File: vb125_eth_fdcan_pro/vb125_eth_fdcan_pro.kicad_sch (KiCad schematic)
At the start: 0 parts

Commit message: Finish schematics.
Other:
- sheet Bus Power ports: added +VIN_DB9; removed none
- sheet CAN Ch1 ports: added +VIN_DB9, FDCAN_RX, FDCAN_TX, TERM_DIS, TERM_EN; removed none
- sheet CAN Ch2: file p7_can_ch2.kicad_sch -> p6_can_ch1.kicad_sch
- sheet CAN Ch2 ports: added FDCAN_RX, FDCAN_TX, TERM_DIS, TERM_EN; removed none
- sheet MCU_H7 ports: added FDCAN1_RX, FDCAN1_TX, FDCAN3_RX, FDCAN3_TX, TERM1_DIS, TERM1_EN, TERM2_DIS, TERM2_EN; removed none
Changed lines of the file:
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@@
     (company "vhrd.tech")
+  )
+  (wire (pts (xy 119.38 90.17) (xy 127 90.17))
+    (stroke (width 0) (type default))
+  )
+  (wire (pts (xy 119.38 92.71) (xy 127 92.71))
+    (stroke (width 0) (type default))
+  )
+  (wire (pts (xy 119.38 111.76) (xy 127 111.76))
+    (stroke (width 0) (type default))
+  )
+  (wire (pts (xy 119.38 114.3) (xy 127 114.3))
+    (stroke (width 0) (type default))
+  )
+  (wire (pts (xy 158.75 106.68) (xy 170.18 106.68))
+    (stroke (width 0) (type default))
+  )
+  (wire (pts (xy 119.38 105.41) (xy 127 105.41))
+    (stroke (width 0) (type default))
+  )
+  (wire (pts (xy 119.38 83.82) (xy 127 83.82))
+    (stroke (width 0) (type default))
+  )
+  (wire (pts (xy 119.38 86.36) (xy 127 86.36))
+    (stroke (width 0) (type default))
+  )
+  (wire (pts (xy 119.38 107.95) (xy 127 107.95))
+    (stroke (width 0) (type default))
   )
   (text_box "TODO:\n--\nabc\n"
@@
     )
   )
-  (sheet (at 170.18 115.57) (size 31.75 7.62) (fields_autoplaced)
-    (stroke (width 0.1524) (type solid))
-    (fill (color 0 0 0 0.0000))
-    (property "Sheetname" "Bus Power" (at 170.18 114.8584 0)
-      (effects (font (size 1.27 1.27)) (justify left bottom))
-    )
-    (property "Sheetfile" "p9_bus_power.kicad_sch" (at 170.18 123.7746 0)
-      (effects (font (size 1.27 1.27)) (justify left top))
+  (sheet (at 127 81.28) (size 31.75 13.97) (fields_autoplaced)
+    (stroke (width 0.1524) (type solid))
+    (fill (color 0 0 0 0.0000))
+    (property "Sheetname" "CAN Ch2" (at 127 80.5684 0)
+      (effects (font (size 1.27 1.27)) (justify left bottom))
+    )
+    (property "Sheetfile" "p6_can_ch1.kicad_sch" (at 127 95.8346 0)
+      (effects (font (size 1.27 1.27)) (justify left top))
+    )
+    (pin "FDCAN_TX" input (at 127 83.82 180)
+      (effects (font (size 1.27 1.27)) (justify left))
+    )
+    (pin "FDCAN_RX" output (at 127 86.36 180)
+      (effects (font (size 1.27 1.27)) (justify left))
+    )
+    (pin "TERM_EN" input (at 127 90.17 180)
+      (effects (font (size 1.27 1.27)) (justify left))
+    )
+    (pin "TERM_DIS" input (at 127 92.71 180)
+      (effects (font (size 1.27 1.27)) (justify left))
+    )
+    (instances
+      (project "vb125_eth_fdcan_pro"
+        (path "/b473bccb-f14c-41d5-b473-137d3ef8ae1e" (page "7"))
+      )
+    )
+  )
+  (sheet (at 170.18 102.87) (size 31.75 7.62) (fields_autoplaced)
+    (stroke (width 0.1524) (type solid))
+    (fill (color 0 0 0 0.0000))
+    (property "Sheetname" "Bus Power" (at 170.18 102.1584 0)
+      (effects (font (size 1.27 1.27)) (justify left bottom))
+    )
+    (property "Sheetfile" "p9_bus_power.kicad_sch" (at 170.18 111.0746 0)
+      (effects (font (size 1.27 1.27)) (justify left top))
+    )
+    (pin "+VIN_DB9" input (at 170.18 106.68 180)
+      (effects (font (size 1.27 1.27)) (justify left))
     )
     (instances
@@
     )
   )
-  (sheet (at 170.18 100.33) (size 31.75 7.62) (fields_autoplaced)
-    (stroke (width 0.1524) (type solid))
-    (fill (color 0 0 0 0.0000))
-    (property "Sheetname" "PoE" (at 170.18 99.6184 0)
-      (effects (font (size 1.27 1.27)) (justify left bottom))
-    )
-    (property "Sheetfile" "p8_poe.kicad_sch" (at 170.18 108.5346 0)
+  (sheet (at 170.18 118.11) (size 31.75 7.62) (fields_autoplaced)
+    (stroke (width 0.1524) (type solid))
+    (fill (color 0 0 0 0.0000))
+    (property "Sheetname" "PoE" (at 170.18 117.3984 0)
+      (effects (font (size 1.27 1.27)) (justify left bottom))
+    )
+    (property "Sheetfile" "p8_poe.kicad_sch" (at 170.18 126.3146 0)
       (effects (font (size 1.27 1.27)) (justify left top))
     )
@@
     )
   )
-  (sheet (at 170.18 85.09) (size 31.75 7.62) (fields_autoplaced)
-    (stroke (width 0.1524) (type solid))
-    (fill (color 0 0 0 0.0000))
-    (property "Sheetname" "CAN Ch1" (at 170.18 84.3784 0)
-      (effects (font (size 1.27 1.27)) (justify left bottom))
-    )
-    (property "Sheetfile" "p6_can_ch1.kicad_sch" (at 170.18 93.2946 0)
-      (effects (font (size 1.27 1.27)) (justify left top))
+  (sheet (at 127 102.87) (size 31.75 13.97) (fields_autoplaced)
+    (stroke (width 0.1524) (type solid))
+    (fill (color 0 0 0 0.0000))
+    (property "Sheetname" "CAN Ch1" (at 127 102.1584 0)
+      (effects (font (size 1.27 1.27)) (justify left bottom))
+    )
+    (property "Sheetfile" "p6_can_ch1.kicad_sch" (at 127 117.4246 0)
+      (effects (font (size 1.27 1.27)) (justify left top))
+    )
+    (pin "FDCAN_TX" input (at 127 105.41 180)
+      (effects (font (size 1.27 1.27)) (justify left))
+    )
+    (pin "FDCAN_RX" output (at 127 107.95 180)
+      (effects (font (size 1.27 1.27)) (justify left))
+    )
+    (pin "+VIN_DB9" output (at 158.75 106.68 0)
+      (effects (font (size 1.27 1.27)) (justify right))
+    )
+    (pin "TERM_EN" input (at 127 111.76 180)
+      (effects (font (size 1.27 1.27)) (justify left))
+    )
+    (pin "TERM_DIS" input (at 127 114.3 180)
+      (effects (font (size 1.27 1.27)) (justify left))
     )
     (instances
@@
     )
   )
-  (sheet (at 170.18 25.4) (size 31.75 7.62) (fields_autoplaced)
-    (stroke (width 0.1524) (type solid))
-    (fill (color 0 0 0 0.0000))
-    (property "Sheetname" "MCU_H7" (at 170.18 24.6884 0)
-      (effects (font (size 1.27 1.27)) (justify left bottom))
-    )
-    (property "Sheetfile" "p2_mcu_h7.kicad_sch" (at 170.18 33.6046 0)
-      (effects (font (size 1.27 1.27)) (justify left top))
+  (sheet (at 87.63 81.28) (size 31.75 35.56) (fields_autoplaced)
+    (stroke (width 0.1524) (type solid))
+    (fill (color 0 0 0 0.0000))
+    (property "Sheetname" "MCU_H7" (at 87.63 80.5684 0)
+      (effects (font (size 1.27 1.27)) (justify left bottom))
+    )
+    (property "Sheetfile" "p2_mcu_h7.kicad_sch" (at 87.63 117.4246 0)
+      (effects (font (size 1.27 1.27)) (justify left top))
+    )
+    (pin "FDCAN3_RX" input (at 119.38 107.95 0)
+      (effects (font (size 1.27 1.27)) (justify right))
+    )
+    (pin "FDCAN3_TX" output (at 119.38 105.41 0)
+      (effects (font (size 1.27 1.27)) (justify right))
+    )
+    (pin "TERM2_EN" output (at 119.38 111.76 0)
+      (effects (font (size 1.27 1.27)) (justify right))
+    )
+    (pin "TERM2_DIS" output (at 119.38 114.3 0)
+      (effects (font (size 1.27 1.27)) (justify right))
+    )
+    (pin "FDCAN1_RX" input (at 119.38 86.36 0)
+      (effects (font (size 1.27 1.27)) (justify right))
+    )
+    (pin "FDCAN1_TX" output (at 119.38 83.82 0)
+      (effects (font (size 1.27 1.27)) (justify right))
+    )
+    (pin "TERM1_EN" output (at 119.38 90.17 0)
+      (effects (font (size 1.27 1.27)) (justify right))
+    )
+    (pin "TERM1_DIS" output (at 119.38 92.71 0)
+      (effects (font (size 1.27 1.27)) (justify right))
     )
     (instances
@@
       )
     )
-  )
-  (sheet (at 207.01 85.09) (size 31.75 7.62) (fields_autoplaced)
-    (stroke (width 0.1524) (type solid))
-    (fill (color 0 0 0 0.0000))
-    (property "Sheetname" "CAN Ch2" (at 207.01 84.3784 0)
-      (effects (font (size 1.27 1.27)) (justify left bottom))
-    )
-    (property "Sheetfile" "p7_can_ch2.kicad_sch" (at 207.01 93.2946 0)
-      (effects (font (size 1.27 1.27)) (justify left top))
-    )
-    (instances
-      (project "vb125_eth_fdcan_pro"
-        (path "/b473bccb-f14c-41d5-b473-137d3ef8ae1e" (page "7"))
-      )
-    )

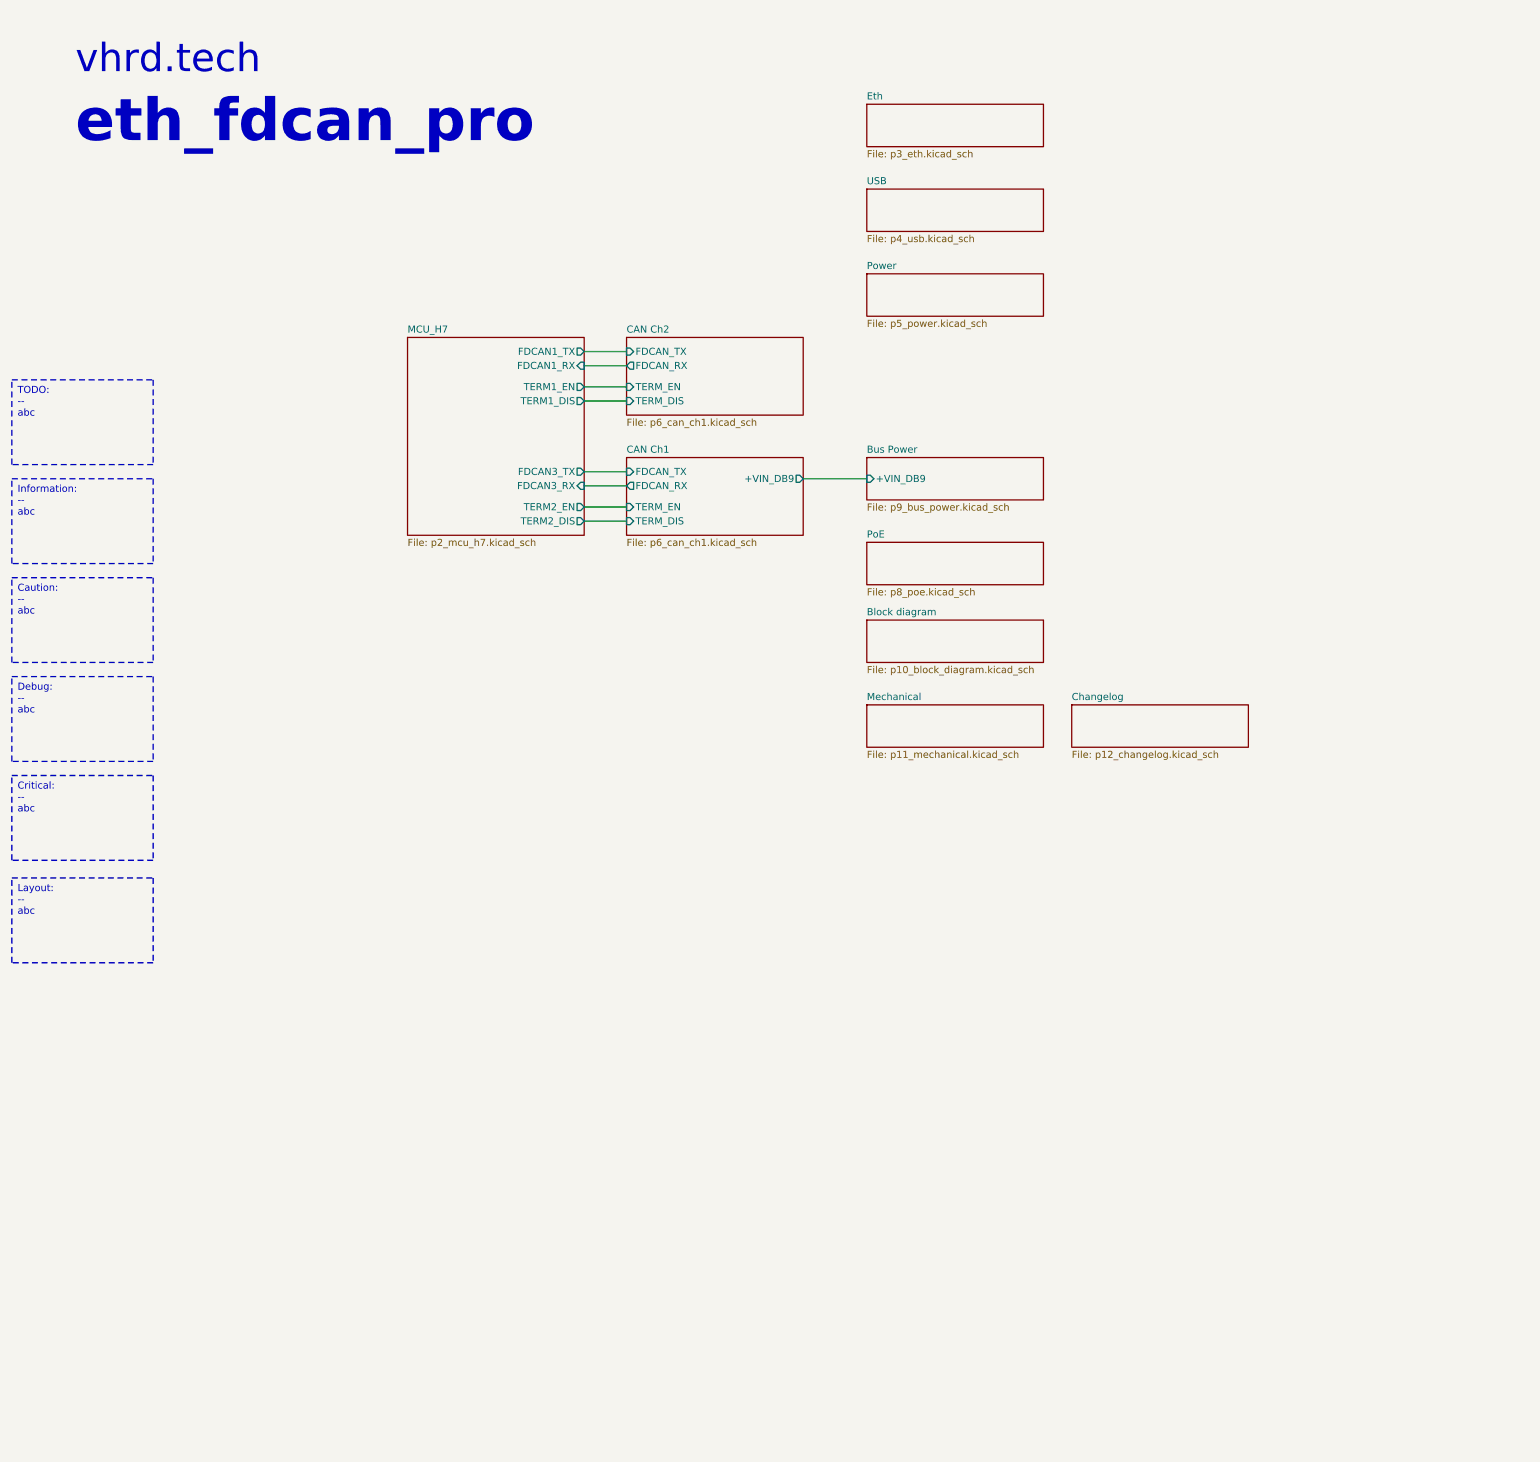
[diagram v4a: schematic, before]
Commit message: Add testpoints and set page templates.
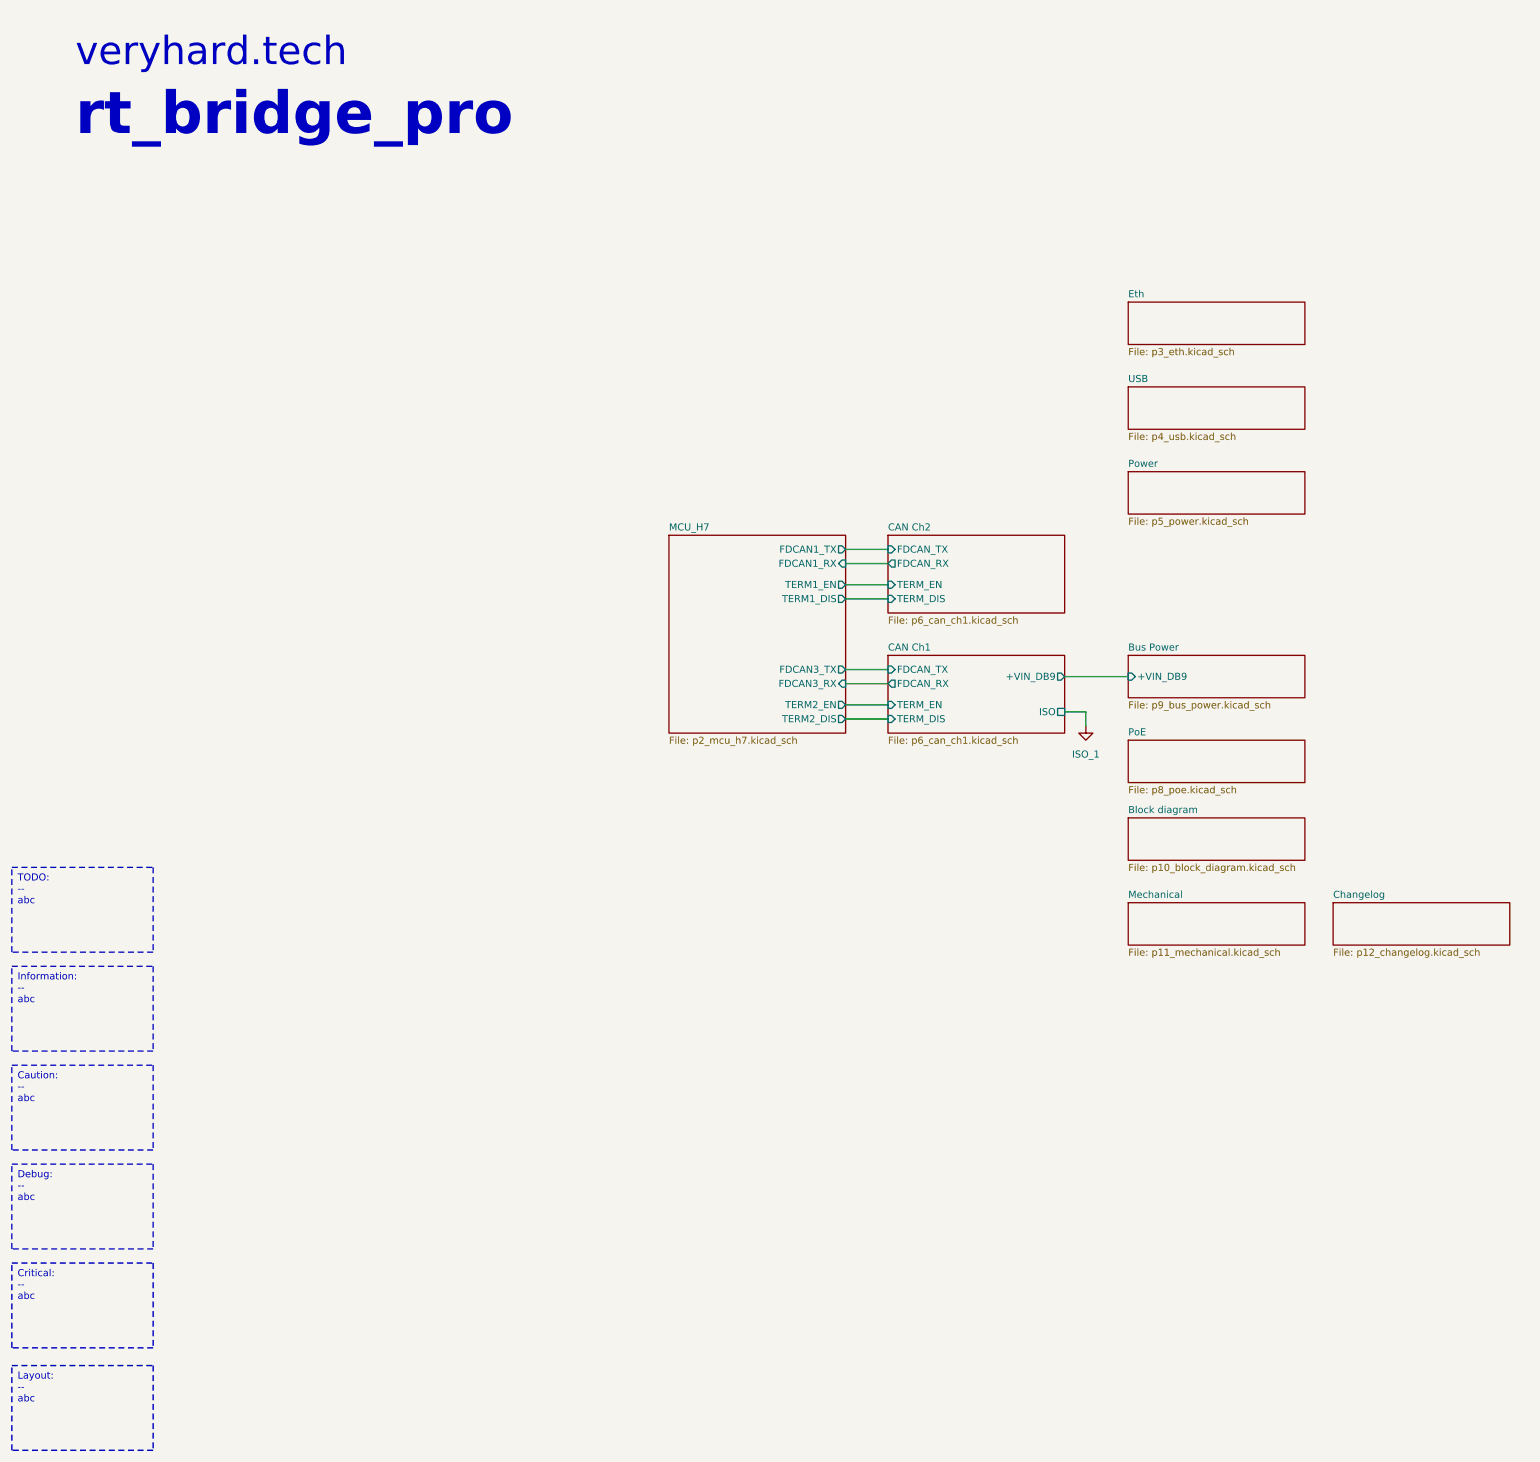
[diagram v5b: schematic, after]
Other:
- sheet CAN Ch1 ports: added ISO; removed none
- note added: "rt_bridge_pro"
- note added: "veryhard.tech"
- note removed: "eth_fdcan_pro"
- note removed: "vhrd.tech"
- company: vhrd.tech -> vhrd.tech AS
- title: (none) -> rt_bridge_pro

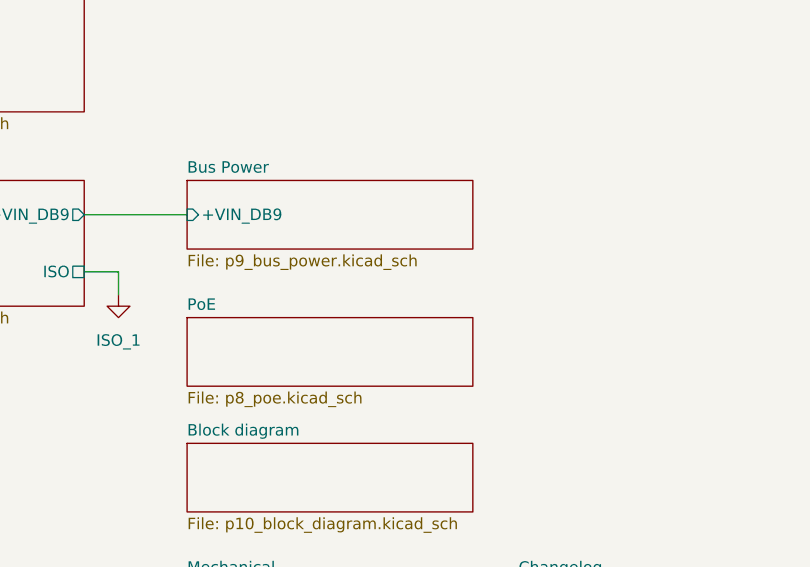
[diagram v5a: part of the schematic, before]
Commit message: Preliminary placement.
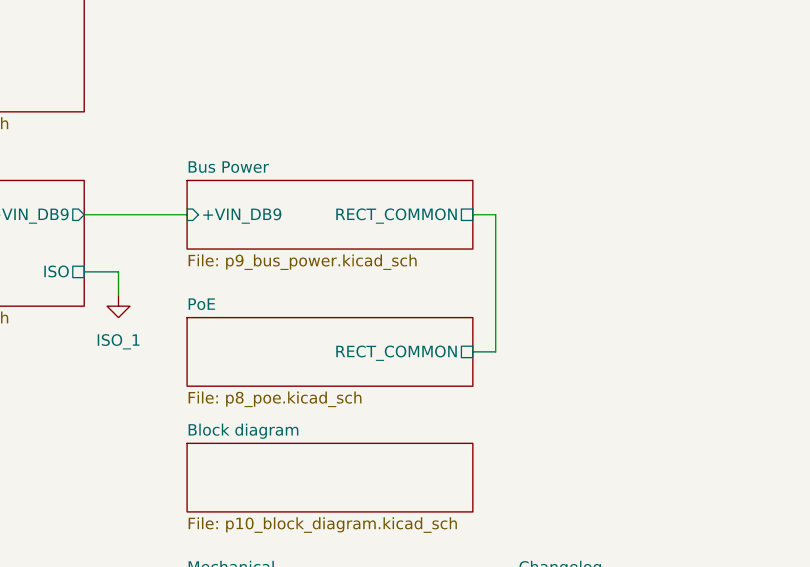
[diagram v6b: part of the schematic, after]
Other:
- sheet Bus Power ports: added RECT_COMMON; removed none
- sheet PoE ports: added RECT_COMMON; removed none
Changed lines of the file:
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@@
+    (stroke (width 0) (type default))
+  )
+  (wire (pts (xy 251.46 157.48) (xy 251.46 142.24))
     (stroke (width 0) (type default))
   )
@@
     (stroke (width 0) (type default))
   )
+  (wire (pts (xy 251.46 142.24) (xy 248.92 142.24))
+    (stroke (width 0) (type default))
+  )
   (wire (pts (xy 166.37 149.86) (xy 173.99 149.86))
     (stroke (width 0) (type default))
   )
   (wire (pts (xy 205.74 142.24) (xy 217.17 142.24))
+    (stroke (width 0) (type default))
+  )
+  (wire (pts (xy 248.92 157.48) (xy 251.46 157.48))
     (stroke (width 0) (type default))
   )
@@
       (effects (font (size 1.27 1.27)) (justify left))
     )
+    (pin "RECT_COMMON" passive (at 248.92 142.24 0)
+      (effects (font (size 1.27 1.27)) (justify right))
+    )
     (instances
       (project "vb125_eth_fdcan_pro"
@@
       (effects (font (size 1.27 1.27)) (justify left top))
     )
-    (instances
+    (pin "RECT_COMMON" passive (at 248.92 157.48 0)
+      (effects (font (size 1.27 1.27)) (justify right))
+    )
+    (instances
